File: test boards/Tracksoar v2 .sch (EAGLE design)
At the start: 48 parts, among them IC1 BME280, IC2 74AHC1G125DBV, Y1 16MHZ

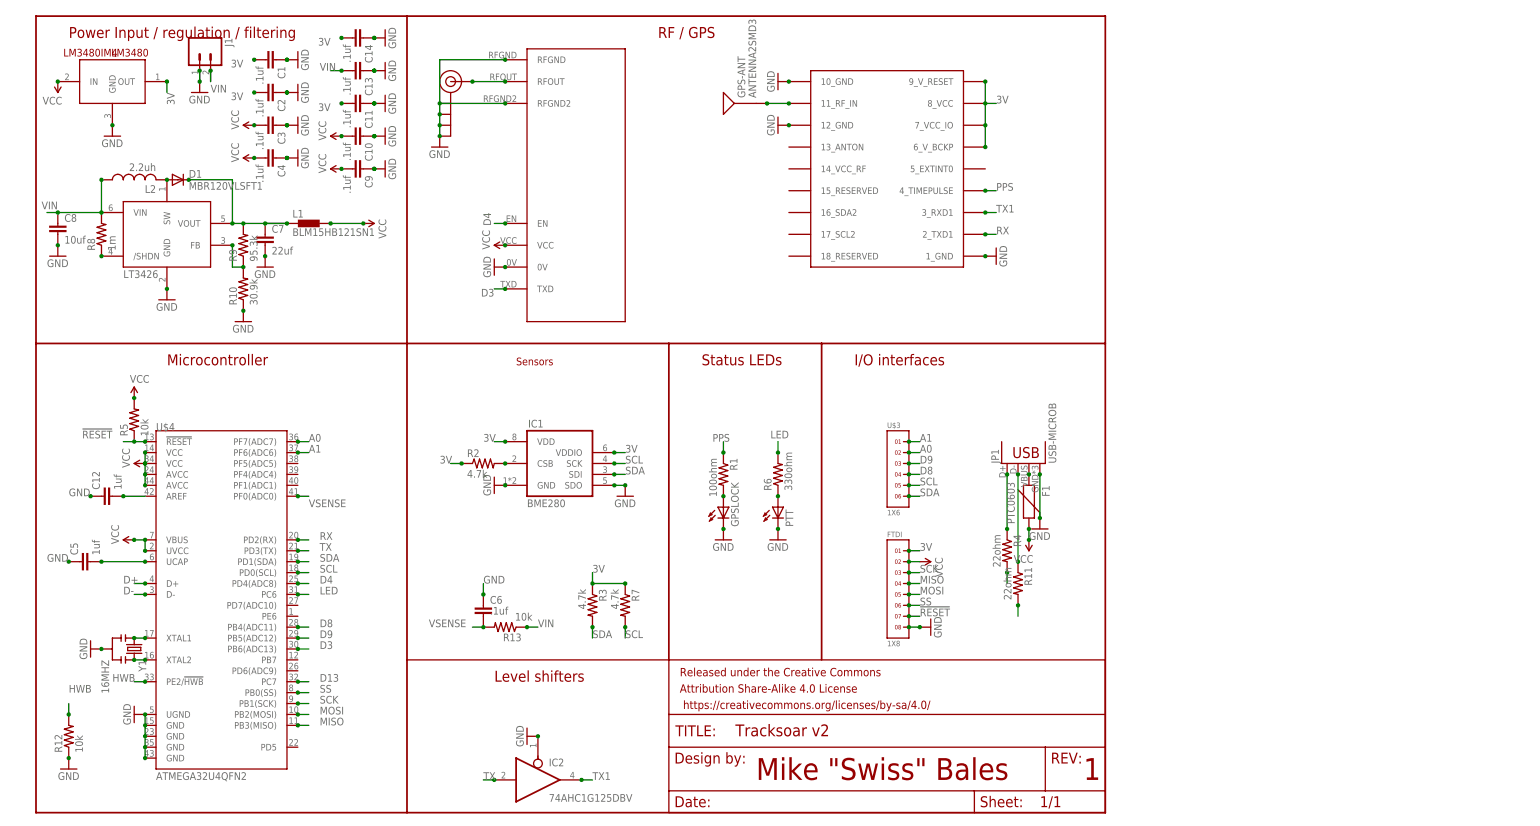
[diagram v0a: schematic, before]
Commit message: removed ldo and level shifter
replaced the 3v ldo with a switching regulator, replaced level shifter with resistor dividers.
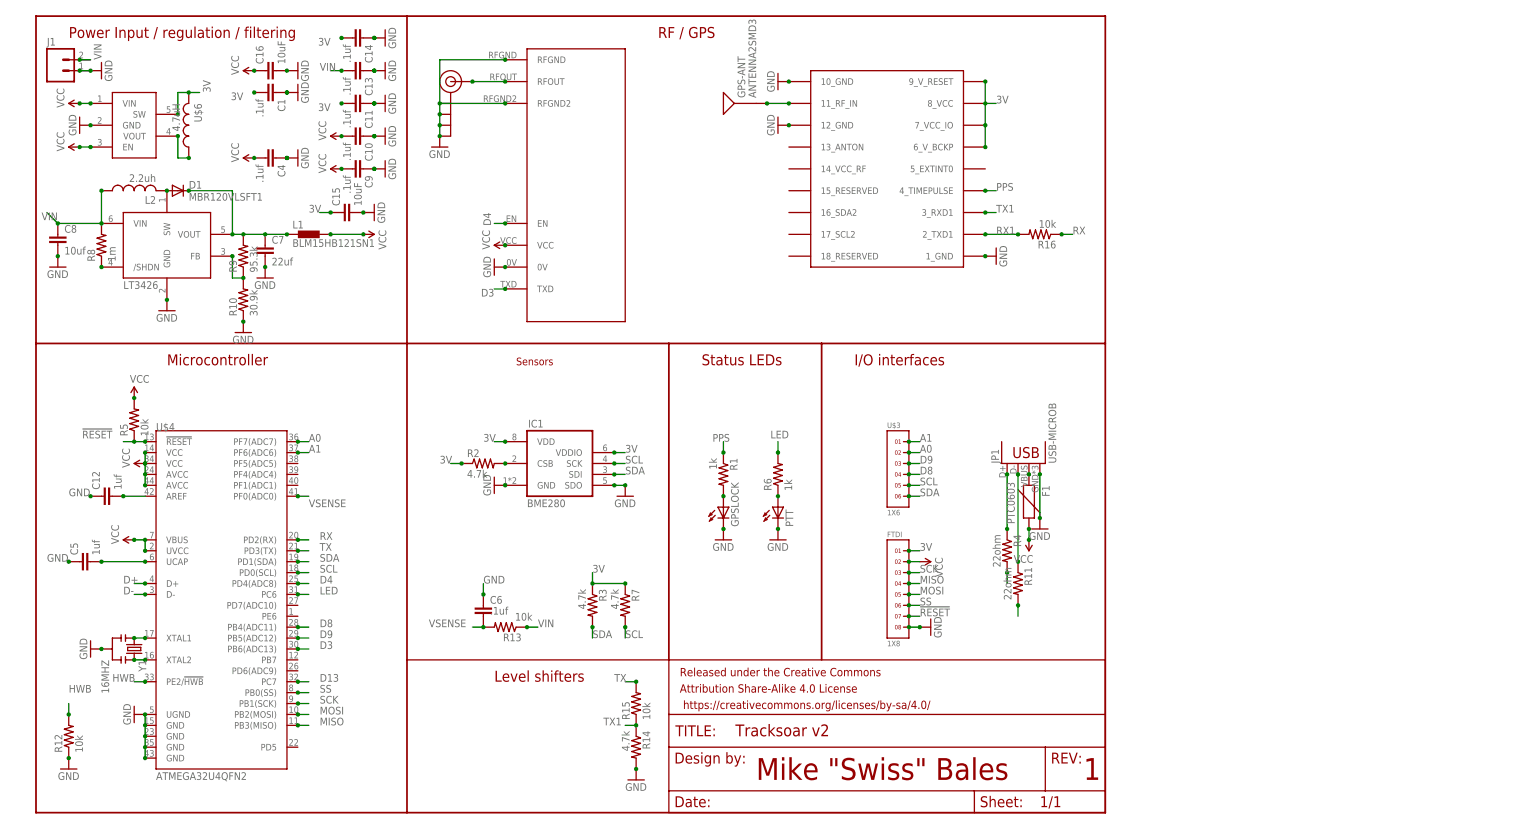
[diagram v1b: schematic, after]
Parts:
- removed C2, C3: .1uf, SparkFun-Capacitors:CAP0402-CAP
- removed IC2: 74AHC1G125DBV, 74xx-little-us:74AHC1G125DBV
- removed LM3480: LM3480IM4, SparkFun-PowerIC:LM3480IM4
- added C15, C16: 10uF, SparkFun-Capacitors:10UF-0603-6.3V-20%
- added R14: 4.7k, adafruit:R-US_R0402
- added R15, R16: 10k, adafruit:R-US_R0402
- added U$5: PAM2305, PAM2305-33:PAM2305-33SOT23-5
- added U$6: 4.7uH, Nordic_nRF:INDUCTOR_0805_N
- R1: value 100ohm -> 1k
- R6: value 330ohm -> 1k
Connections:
- new net N$18: U$5.VOUT, U$6.1
- new net RX1: R16.2, U$1.2_TXD1
- net 3V: now also C15.1, U$5.SW, U$6.2; no longer C2.2, LM3480.OUT
- net GND: now also C15.2, C16.2, R14.2, U$5.GND; no longer C2.1, C3.1, IC2A.OE, LM3480.GND
- net RX: now also R16.1; no longer U$1.2_TXD1
- net TX: now also R15.2; no longer IC2A.I
- net TX1: now also R14.1, R15.1; no longer IC2A.O
- net VCC: now also C16.1, U$5.EN, U$5.VIN; no longer C3.2, LM3480.IN
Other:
- moved on the sheet: C1, C7, C8, D1, J1, L1, L2, R10, R8, R9

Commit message: updated rf paths
seperated RF GND from GND and coupled via an inductor. Implemented path cleanups. Made all RF impedence matched.
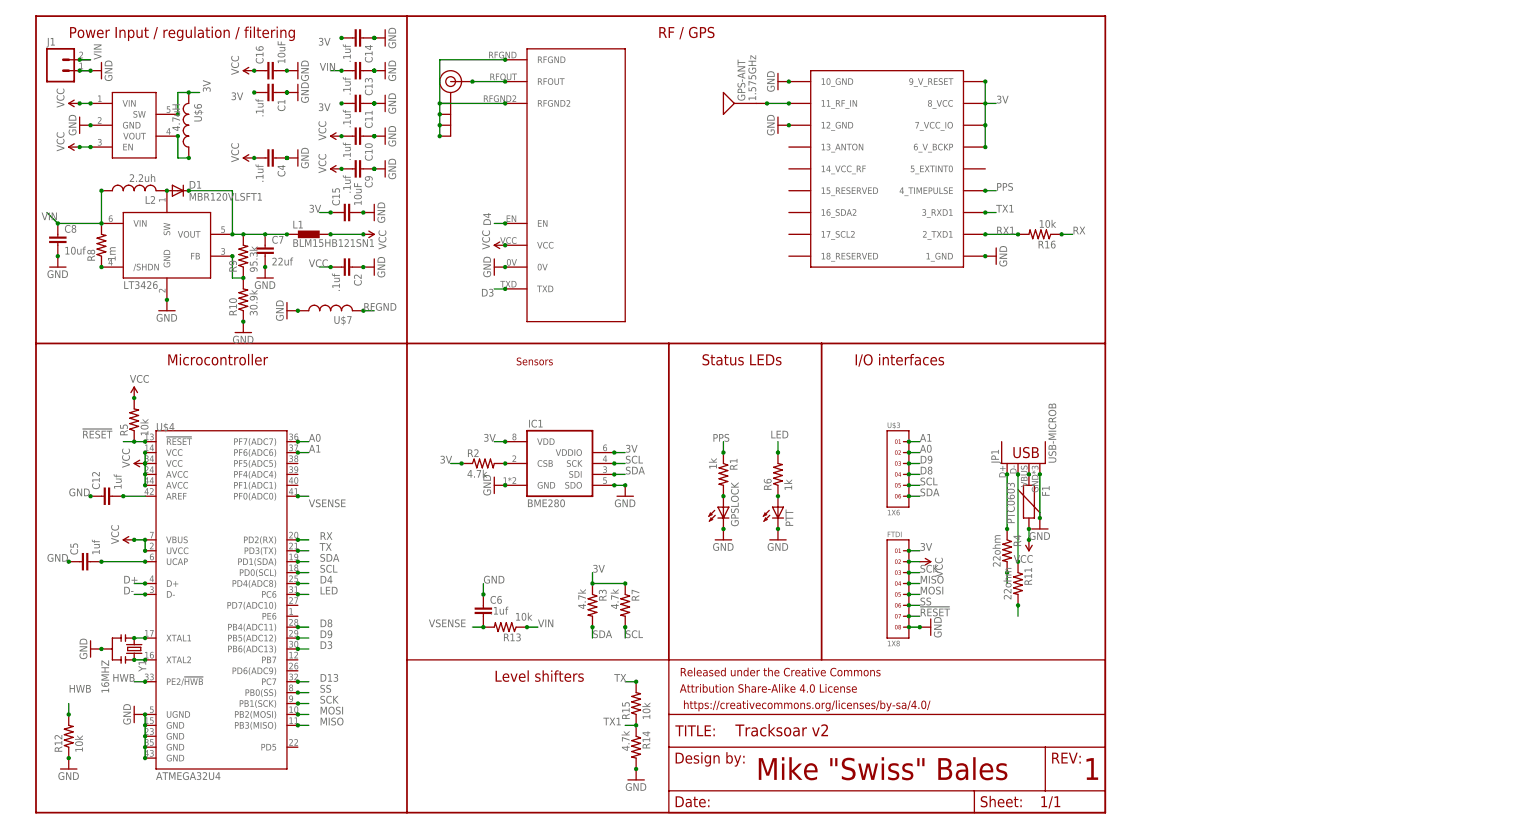
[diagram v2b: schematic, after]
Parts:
- added C2: .1uf, SparkFun-Capacitors:CAP0402-CAP
- added U$7: (no value), Nordic_nRF:INDUCTOR_0402_N
- GPS-ANT: value ANTENNA2SMD3 -> 1.575GHz; device SparkFun-RF:ANTENNA2SMD3 -> SparkFun-GPS:ANTENNAGPS-2X7MM
- U$4: value ATMEGA32U4QFN2 -> ATMEGA32U4
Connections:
- new net RFGND: J$1.GND@0, J$1.GND@1, J$1.GND@2, J$1.GND@3, U$2.RFGND, U$2.RFGND2, U$7.2
- net GND: now also C2.1, U$7.1; no longer J$1.GND@0, J$1.GND@1, J$1.GND@2, J$1.GND@3, U$2.RFGND, U$2.RFGND2
- net VCC: now also C2.2
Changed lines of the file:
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@@
 <part name="U$2" library="Ava" deviceset="RADIOMETRIX-HX1" device=""/>
 <part name="J$1" library="SparkFun-Connectors" deviceset="SMA_EDGE" device=""/>
-<part name="GND4" library="SparkFun-Aesthetics" deviceset="GND" device=""/>
 <part name="SUPPLY3" library="SparkFun-Aesthetics" deviceset="VCC" device=""/>
 <part name="GND7" library="SparkFun-Aesthetics" deviceset="GND" device=""/>
@@
 <part name="GND29" library="SparkFun-Aesthetics" deviceset="GND" device=""/>
 <part name="GND30" library="SparkFun-Aesthetics" deviceset="GND" device=""/>
-<part name="GPS-ANT" library="SparkFun-RF" deviceset="ANTENNA2" device="SMD3"/>
+<part name="GPS-ANT" library="SparkFun-GPS" library_urn="urn:adsk.eagle:library:518" deviceset="ANTENNA" device="GPS-2X7MM" package3d_urn="urn:adsk.eagle:package:38594/1" value="1.575GHz"/>
 <part name="FTDI" library="headers(2mm)" deviceset="1X8" device=""/>
 <part name="GND5" library="SparkFun-Aesthetics" deviceset="GND" device=""/>
@@
 <part name="GND6" library="SparkFun-Aesthetics" deviceset="GND" device=""/>
 <part name="R2" library="adafruit" deviceset="R-US_" device="R0402" value="4.7k"/>
-<part name="U$4" library="SparkFun-DigitalIC" deviceset="ATMEGA32U4" device="QFN2"/>
+<part name="U$4" library="SparkFun-DigitalIC" deviceset="ATMEGA32U4" device="QFN2" value="ATMEGA32U4"/>
 <part name="GND11" library="SparkFun-Aesthetics" deviceset="GND" device=""/>
 <part name="SUPPLY6" library="SparkFun-Aesthetics" deviceset="VCC" device=""/>
@@
 <part name="GND1" library="SparkFun-Aesthetics" deviceset="GND" device=""/>
 <part name="R16" library="adafruit" deviceset="R-US_" device="R0402" value="10k"/>
+<part name="U$7" library="Nordic_nRF" library_urn="urn:adsk.eagle:library:169009" deviceset="INDUCTOR" device="_0402_N" package3d_urn="urn:adsk.eagle:package:169047/1"/>
+<part name="GND17" library="SparkFun-Aesthetics" deviceset="GND" device=""/>
+<part name="C2" library="SparkFun-Capacitors" deviceset="CAP" device="0402-CAP" value=".1uf"/>
+<part name="GND2" library="SparkFun-Aesthetics" deviceset="GND" device=""/>
 </parts>
 <sheets>
@@
 <instance part="U$2" gate="G$1" x="111.76" y="134.62" rot="R270"/>
 <instance part="J$1" gate="1" x="96.52" y="170.18"/>
-<instance part="GND4" gate="1" x="93.98" y="154.94"/>
 <instance part="SUPPLY3" gate="G$1" x="109.22" y="132.08" rot="R90"/>
 <instance part="GND7" gate="1" x="106.68" y="127" rot="R270"/>
@@
 <instance part="GND1" gate="1" x="139.7" y="7.62"/>
 <instance part="R16" gate="G$1" x="233.68" y="134.62" rot="R180"/>
+<instance part="U$7" gate="L$1" x="68.58" y="116.84" rot="R90"/>
+<instance part="GND17" gate="1" x="58.42" y="116.84" rot="R270"/>
+<instance part="C2" gate="G$1" x="71.12" y="127" rot="R270"/>
+<instance part="GND2" gate="1" x="78.74" y="127" rot="R90"/>
 </instances>
 <busses>
@@
 <nets>
 <net name="GND" class="0">
-<segment>
-<pinref part="J$1" gate="1" pin="GND@3"/>
-<pinref part="GND4" gate="1" pin="GND"/>
-<pinref part="J$1" gate="1" pin="GND@0"/>
-<wire x1="93.98" y1="165.1" x2="93.98" y2="162.56" width="0.1524" layer="91"/>
-<junction x="93.98" y="165.1"/>
-<pinref part="J$1" gate="1" pin="GND@1"/>
-<junction x="93.98" y="162.56"/>
-<wire x1="93.98" y1="162.56" x2="93.98" y2="160.02" width="0.1524" layer="91"/>
-<pinref part="J$1" gate="1" pin="GND@2"/>
-<junction x="93.98" y="160.02"/>
-<wire x1="93.98" y1="160.02" x2="93.98" y2="157.48" width="0.1524" layer="91"/>
-<junction x="93.98" y="157.48"/>
-<pinref part="U$2" gate="G$1" pin="RFGND2"/>
-<wire x1="109.22" y1="165.1" x2="93.98" y2="165.1" width="0.1524" layer="91"/>
-<pinref part="U$2" gate="G$1" pin="RFGND"/>
-<wire x1="93.98" y1="165.1" x2="93.98" y2="175.26" width="0.1524" layer="91"/>
-<wire x1="93.98" y1="175.26" x2="109.22" y2="175.26" width="0.1524" layer="91"/>
-<junction x="109.22" y="175.26"/>
-<junction x="109.22" y="165.1"/>
-</segment>
 <segment>
 <pinref part="U$2" gate="G$1" pin="0V"/>
@@
 <junction x="139.7" y="10.16"/>
 </segment>
+<segment>
+<pinref part="U$7" gate="L$1" pin="1"/>
+<pinref part="GND17" gate="1" pin="GND"/>
+<junction x="60.96" y="116.84"/>
+</segment>
+<segment>
+<pinref part="C2" gate="G$1" pin="1"/>
+<pinref part="GND2" gate="1" pin="GND"/>
+<junction x="76.2" y="127"/>
+</segment>
 </net>
 <net name="D3" class="0">
@@
 <pinref part="SUPPLY2" gate="G$1" pin="VCC"/>
 <junction x="50.8" y="172.72"/>
+</segment>
+<segment>
+<pinref part="C2" gate="G$1" pin="2"/>
+<wire x1="68.58" y1="127" x2="66.04" y2="127" width="0.1524" layer="91"/>
+<junction x="68.58" y="127"/>
+<label x="63.5" y="127" size="1.778" layer="95"/>
 </segment>
 </net>
@@
 </segment>
 </net>
+<net name="RFGND" class="0">
+<segment>
+<pinref part="J$1" gate="1" pin="GND@3"/>
+<pinref part="J$1" gate="1" pin="GND@0"/>
+<wire x1="93.98" y1="165.1" x2="93.98" y2="162.56" width="0.1524" layer="91"/>
+<junction x="93.98" y="165.1"/>
+<pinref part="J$1" gate="1" pin="GND@1"/>
+<junction x="93.98" y="162.56"/>
+<wire x1="93.98" y1="162.56" x2="93.98" y2="160.02" width="0.1524" layer="91"/>
+<pinref part="J$1" gate="1" pin="GND@2"/>
+<junction x="93.98" y="160.02"/>
+<wire x1="93.98" y1="160.02" x2="93.98" y2="157.48" width="0.1524" layer="91"/>
+<pinref part="U$2" gate="G$1" pin="RFGND2"/>
+<wire x1="109.22" y1="165.1" x2="93.98" y2="165.1" width="0.1524" layer="91"/>
+<pinref part="U$2" gate="G$1" pin="RFGND"/>
+<wire x1="93.98" y1="165.1" x2="93.98" y2="175.26" width="0.1524" layer="91"/>
+<wire x1="93.98" y1="175.26" x2="109.22" y2="175.26" width="0.1524" layer="91"/>
+<junction x="109.22" y="175.26"/>
+<junction x="109.22" y="165.1"/>
+<junction x="93.98" y="157.48"/>
+</segment>
+<segment>
+<pinref part="U$7" gate="L$1" pin="2"/>
+<wire x1="76.2" y1="116.84" x2="78.74" y2="116.84" width="0.1524" layer="91"/>
+<label x="76.2" y="116.84" size="1.778" layer="95"/>
+<junction x="76.2" y="116.84"/>
+</segment>
+</net>

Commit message: added buck regulator
swapped the linear regulator for a buck converter.
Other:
- moved on the sheet: C2
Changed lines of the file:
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@@
 <instance part="U$7" gate="L$1" x="68.58" y="116.84" rot="R90"/>
 <instance part="GND17" gate="1" x="58.42" y="116.84" rot="R270"/>
-<instance part="C2" gate="G$1" x="71.12" y="127" rot="R270"/>
-<instance part="GND2" gate="1" x="78.74" y="127" rot="R90"/>
+<instance part="C2" gate="G$1" x="53.34" y="160.02" rot="R270"/>
+<instance part="GND2" gate="1" x="60.96" y="160.02" rot="R90"/>
 </instances>
 <busses>
@@
 <pinref part="C2" gate="G$1" pin="1"/>
 <pinref part="GND2" gate="1" pin="GND"/>
-<junction x="76.2" y="127"/>
+<junction x="58.42" y="160.02"/>
 </segment>
 </net>
@@
 <segment>
 <pinref part="C2" gate="G$1" pin="2"/>
-<wire x1="68.58" y1="127" x2="66.04" y2="127" width="0.1524" layer="91"/>
-<junction x="68.58" y="127"/>
-<label x="63.5" y="127" size="1.778" layer="95"/>
+<wire x1="50.8" y1="160.02" x2="48.26" y2="160.02" width="0.1524" layer="91"/>
+<junction x="50.8" y="160.02"/>
+<label x="45.72" y="160.02" size="1.778" layer="95"/>
 </segment>
 </net>

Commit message: fixed 3v reg
the 3v reg wiring was corrected and output cap moved closer to the regulator.
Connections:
- removed net N$18: U$5.VOUT, U$6.1
- new net N$21: U$5.SW, U$6.2
- net 3V: now also U$5.VOUT, U$6.1; no longer U$5.SW, U$6.2
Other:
- moved on the sheet: U$6
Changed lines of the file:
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@@
 <?xml version="1.0" encoding="utf-8"?>
 <!DOCTYPE eagle SYSTEM "eagle.dtd">
-<eagle version="8.7.0">
+<eagle version="8.6.3">
 <drawing>
 <settings>
@@
 <instance part="GND23" gate="1" x="7.62" y="10.16"/>
 <instance part="U$5" gate="G$1" x="25.4" y="165.1" rot="R90"/>
-<instance part="U$6" gate="L$1" x="35.56" y="160.02" rot="R180"/>
+<instance part="U$6" gate="L$1" x="35.56" y="172.72" rot="R270"/>
 <instance part="SUPPLY11" gate="G$1" x="10.16" y="165.1" rot="R90"/>
 <instance part="SUPPLY12" gate="G$1" x="10.16" y="154.94" rot="R90"/>
@@
 </segment>
 <segment>
-<pinref part="U$5" gate="G$1" pin="SW"/>
-<pinref part="U$6" gate="L$1" pin="2"/>
-<wire x1="33.02" y1="162.56" x2="33.02" y2="167.64" width="0.1524" layer="91"/>
-<wire x1="33.02" y1="167.64" x2="35.56" y2="167.64" width="0.1524" layer="91"/>
-<wire x1="35.56" y1="167.64" x2="38.1" y2="167.64" width="0.1524" layer="91"/>
-<junction x="33.02" y="162.56"/>
-<junction x="35.56" y="167.64"/>
-<label x="40.64" y="167.64" size="1.778" layer="95" rot="R90"/>
-</segment>
-<segment>
 <pinref part="C15" gate="G$1" pin="1"/>
 <wire x1="68.58" y1="139.7" x2="66.04" y2="139.7" width="0.1524" layer="91"/>
 <junction x="68.58" y="139.7"/>
 <label x="63.5" y="139.7" size="1.778" layer="95"/>
+</segment>
+<segment>
+<pinref part="U$5" gate="G$1" pin="VOUT"/>
+<wire x1="33.02" y1="157.48" x2="43.18" y2="157.48" width="0.1524" layer="91"/>
+<pinref part="U$6" gate="L$1" pin="1"/>
+<wire x1="43.18" y1="157.48" x2="43.18" y2="172.72" width="0.1524" layer="91"/>
+<wire x1="43.18" y1="172.72" x2="45.72" y2="172.72" width="0.1524" layer="91"/>
+<junction x="33.02" y="157.48"/>
+<junction x="43.18" y="172.72"/>
 </segment>
 </net>
@@
 <junction x="60.96" y="83.82"/>
 <label x="63.5" y="83.82" size="1.778" layer="95"/>
-</segment>
-</net>
-<net name="N$18" class="0">
-<segment>
-<pinref part="U$6" gate="L$1" pin="1"/>
-<pinref part="U$5" gate="G$1" pin="VOUT"/>
-<wire x1="35.56" y1="152.4" x2="33.02" y2="152.4" width="0.1524" layer="91"/>
-<wire x1="33.02" y1="152.4" x2="33.02" y2="157.48" width="0.1524" layer="91"/>
-<junction x="33.02" y="157.48"/>
-<junction x="35.56" y="152.4"/>
 </segment>
 </net>
@@
 </segment>
 </net>
+<net name="N$21" class="0">
+<segment>
+<pinref part="U$5" gate="G$1" pin="SW"/>
+<wire x1="33.02" y1="162.56" x2="33.02" y2="170.18" width="0.1524" layer="91"/>
+<wire x1="33.02" y1="170.18" x2="27.94" y2="170.18" width="0.1524" layer="91"/>
+<pinref part="U$6" gate="L$1" pin="2"/>
+<wire x1="27.94" y1="170.18" x2="27.94" y2="172.72" width="0.1524" layer="91"/>
+<junction x="33.02" y="162.56"/>
+<junction x="27.94" y="172.72"/>
+</segment>
+</net>
